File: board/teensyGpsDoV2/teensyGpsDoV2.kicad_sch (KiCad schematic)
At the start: 17 parts, among them J1 Barrel_Jack, J2 NPPN042AFCN-RC, SW1 SW_SPDT, U1 Teensy4.0, U2 LT1086-5.0, U3 DAC8550IxDGK, X1 OSC5A2B02

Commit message: Schematic WIP
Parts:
- added C5, C6: 1uF, symbol Device:C_Small_US
- added R7: 100, Resistor_THT:R_Axial_DIN0207_L6.3mm_D2.5mm_P7.62mm_Horizontal, symbol Device:R
- added TP1: 10 MHz TP, TestPoint:TestPoint_Pad_D2.0mm, symbol Connector:TestPoint
- added TP2: 5V TP, TestPoint:TestPoint_Pad_D2.0mm, symbol Connector:TestPoint
- added TP3: 1PPS TP, TestPoint:TestPoint_Pad_D2.0mm, symbol Connector:TestPoint
- added TP4: OSC VREF TP, TestPoint:TestPoint_Pad_D2.0mm, symbol Connector:TestPoint
- added U4: MCP1700x-330xxTO, Package_TO_SOT_THT:TO-92_Inline, symbol Regulator_Linear:MCP1700x-330xxTO
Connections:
- net +5V: now also C5.1, TP2.1, U4.2 (VI)
- net 10 MHz: now also R6.2, U1.26 (19_A5_SCL0)
- net GND: now also C5.2, C6.2, U4.1 (GND)
- net pps: now also U1.25 (18_A4_SDA0), R7.1, TP3.1; no longer J2.6, U1.9 (7_RX2_OUT1A)
- net at R1.2, R2.1, R6.1: now also TP1.1
- net at U1.11 (9_OUT1C): no longer R6.2
- net OSC VCTRL: now reaches U3.3 (V_{FB}), U3.4 (V_{OUT}), X1.3 (VCTRL)
- net OSC VCTRL: now also TP4.1
- net DAC VREF: now reaches U3.2 (V_{REF})
- net DAC VREF: now also C6.1, U4.3 (VO)
- new net: J2.6, R7.2
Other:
- note added: "1: VDD 2: VAnt 3: TxD 4: NC 5: RxD 6: PPS 7: NC 8: GND"
- moved on the sheet: J2, R1, R2, R6, U1, X1

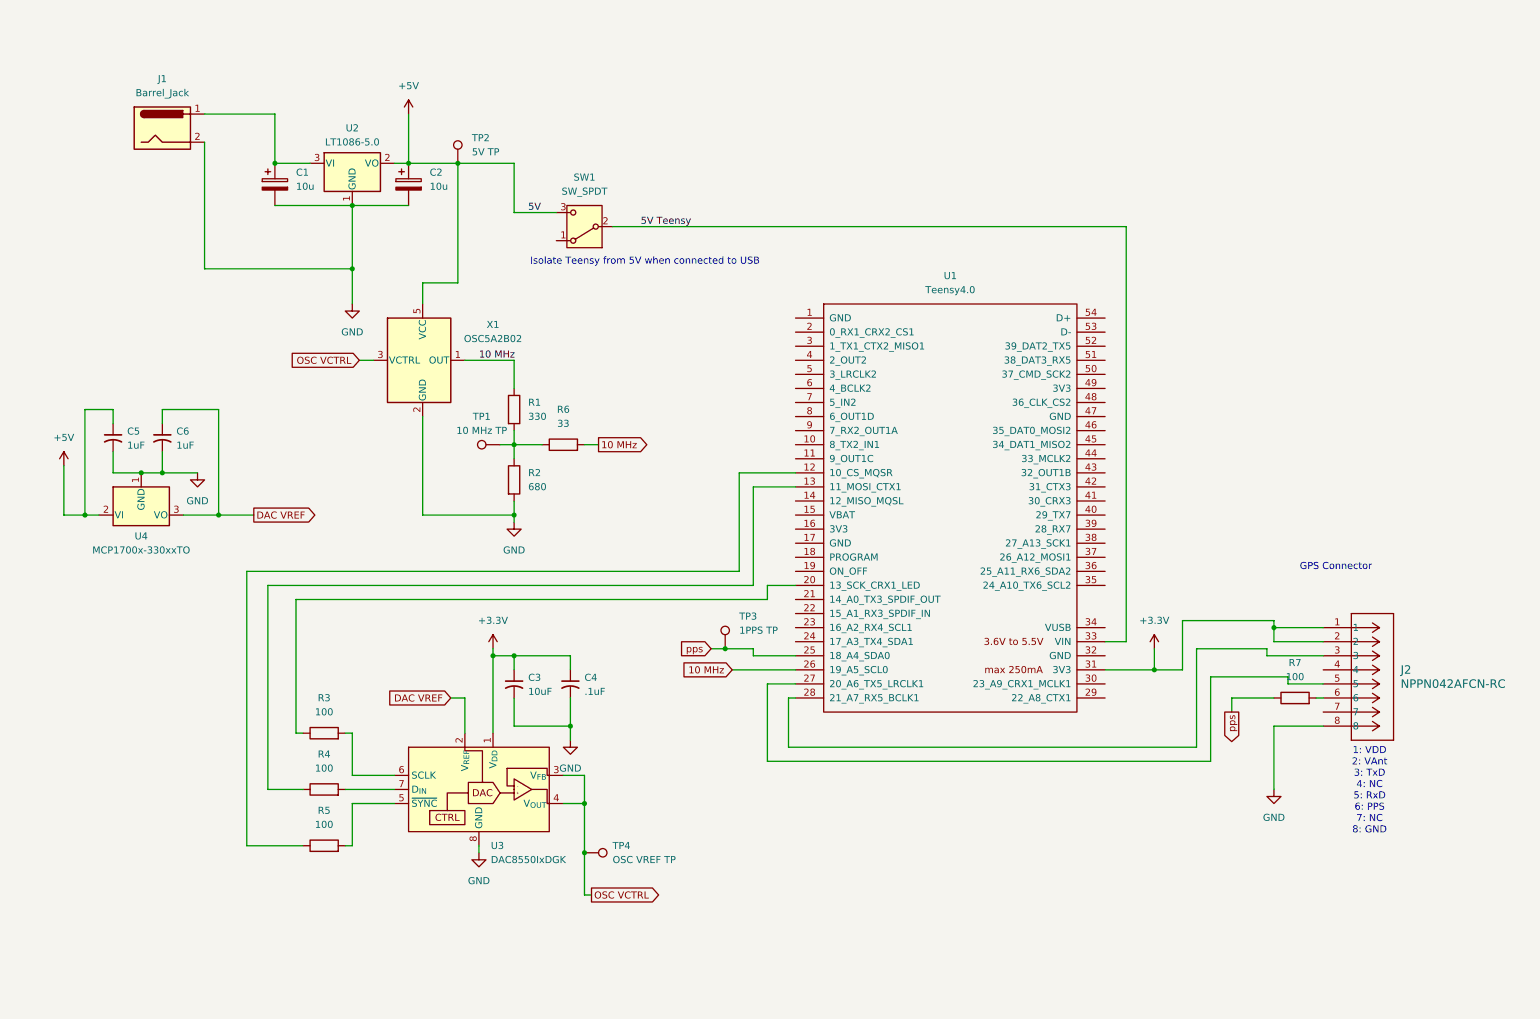
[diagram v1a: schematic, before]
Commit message: WIP, moved libraries to allow wire1 instead of wire modification. Lots of tuning. LCD optimations
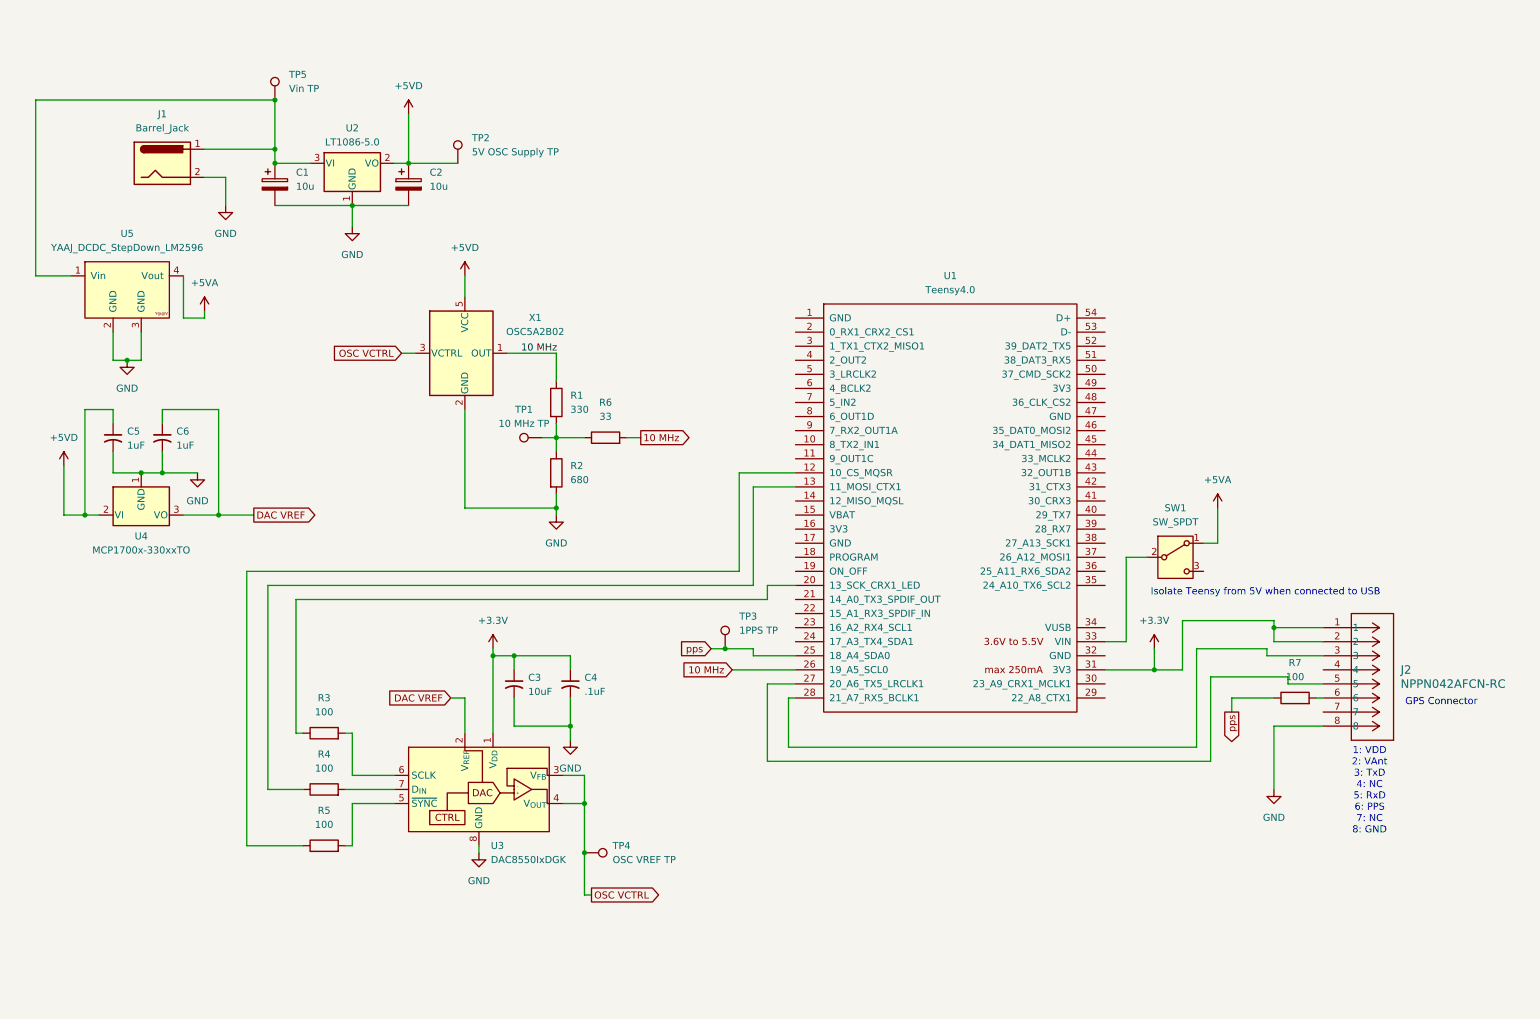
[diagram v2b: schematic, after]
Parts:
- added TP5: Vin TP, TestPoint:TestPoint_Pad_D2.0mm, symbol Connector:TestPoint
- added U5: YAAJ_DCDC_StepDown_LM2596, LM2596_Module:YAAJ_DCDC_StepDown_LM2596, symbol LM2596_Module:YAAJ_DCDC_StepDown_LM2596
- TP2: value 5V TP -> 5V OSC Supply TP
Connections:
- net GND: now also U5.2 (GND), U5.3 (GND)
- net at C1.1, J1.1, U2.3 (VI): now also TP5.1, U5.1 (Vin)
- net +5VA: now reaches SW1.1 (A)
- net +5VA: now also U5.4 (Vout)
- net +5V renamed +5VD
- net +5VD: no longer SW1.3 (C)
- net 5V Teensy: no longer names the net of SW1.2 (B), U1.33 (VIN)
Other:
- moved on the sheet: J1, R1, R2, R6, SW1, TP1, X1

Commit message: mobile update
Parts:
- added FB1, FB2: 133 @ 100 MHz, symbol Device:FerriteBead_Small
- added U6: 74HC14, Package_DIP:DIP-14_W7.62mm_Socket, symbol 74xx:74HC14
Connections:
- net +3.3V: now also FB1.1; no longer C3.1, C4.1, U3.1 (V_{DD})
- net +5VD: now also FB2.1; no longer X1.5 (VCC)
- new net: C3.1, C4.1, FB1.2, U3.1 (V_{DD})
- new net: FB2.2, X1.5 (VCC)

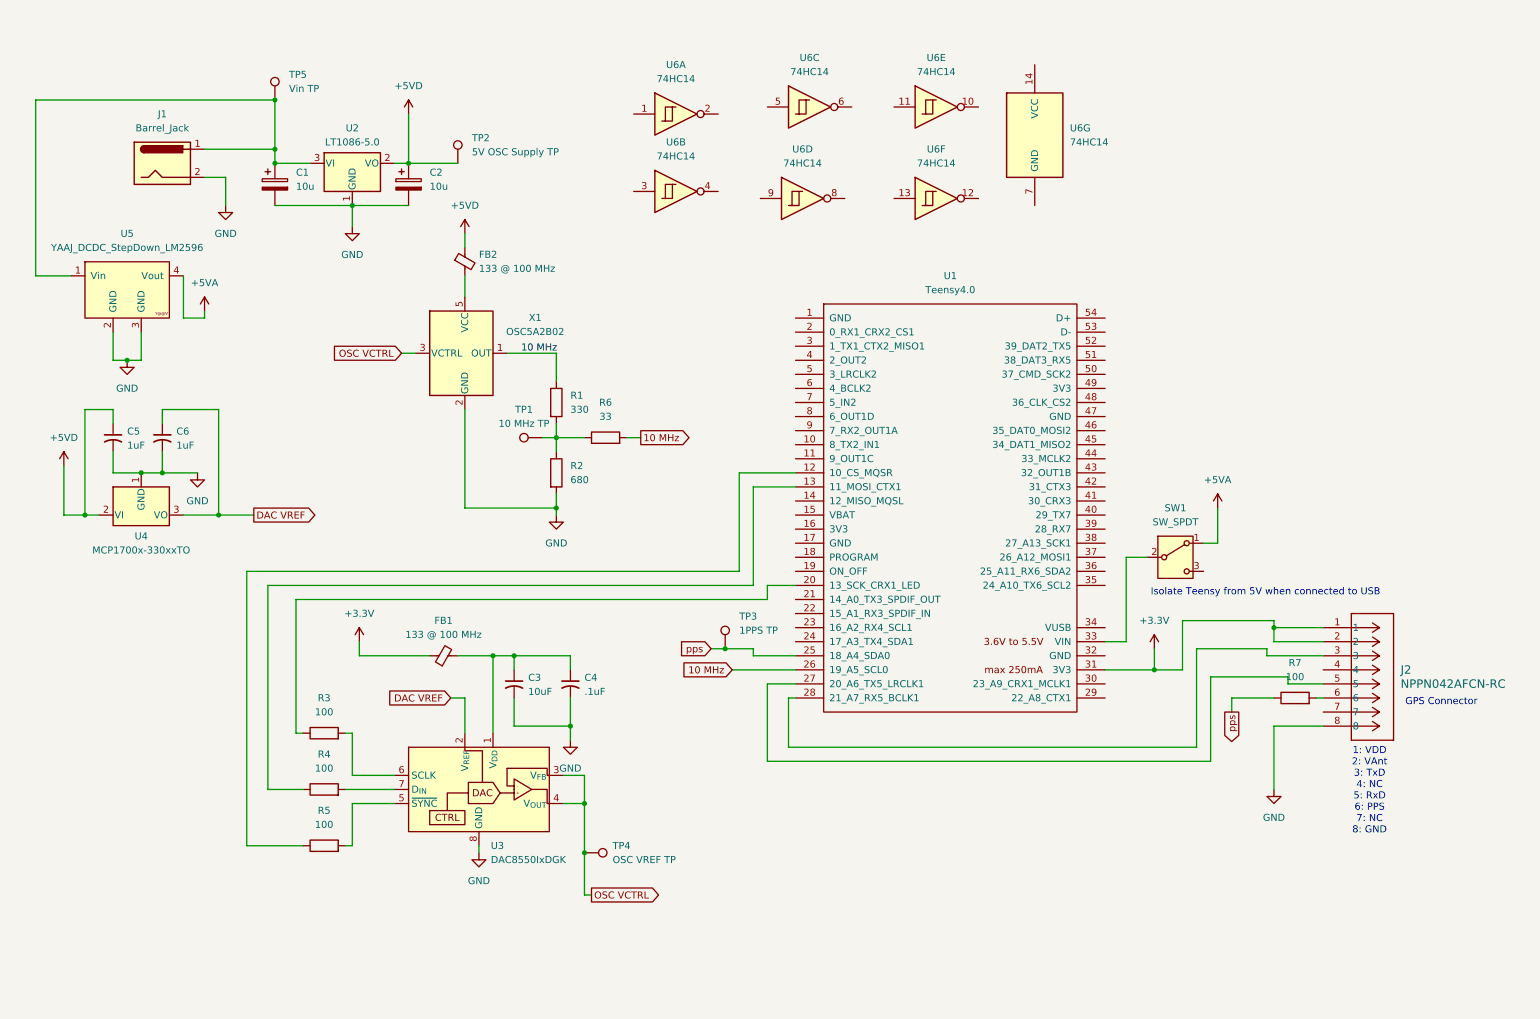
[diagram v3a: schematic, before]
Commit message: wip on schematic. Added PWM option instead of DAC
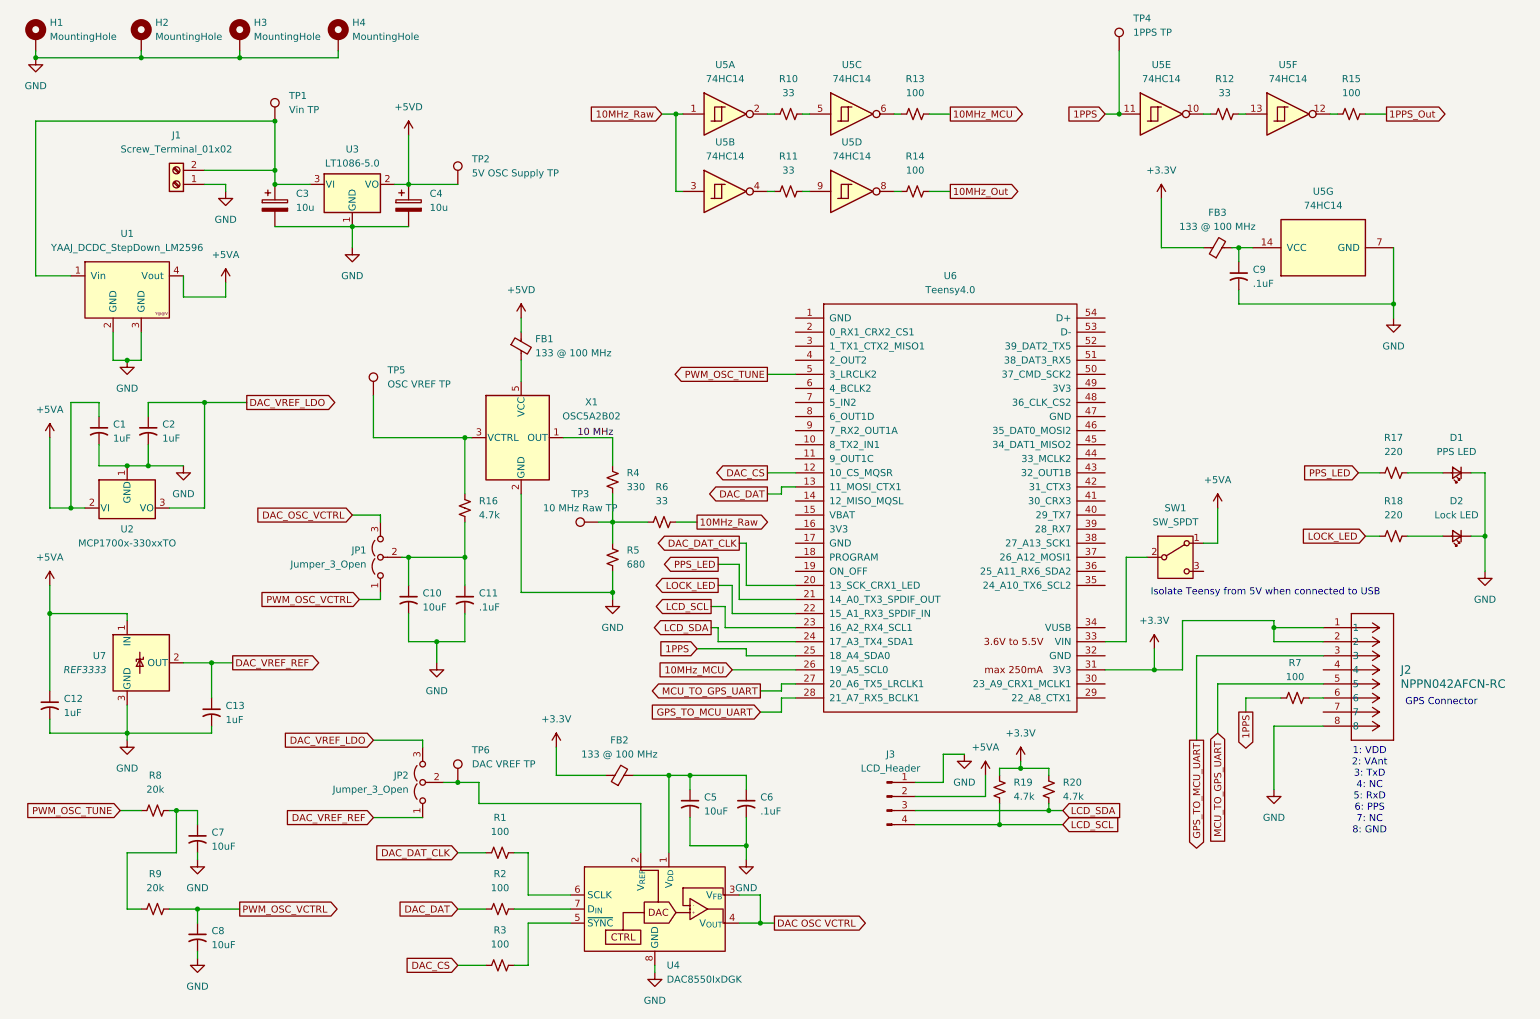
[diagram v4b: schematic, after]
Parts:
- removed J1: Barrel_Jack, Connector_BarrelJack:BarrelJack_SwitchcraftConxall_RAPC10U_Horizontal, symbol Connector:Barrel_Jack
- removed R1: 330, Resistor_THT:R_Axial_DIN0207_L6.3mm_D2.5mm_P7.62mm_Horizontal, symbol Device:R
- removed R2: 680, symbol Device:R
- removed R3, R4, R5, R7: 100, Resistor_THT:R_Axial_DIN0207_L6.3mm_D2.5mm_P7.62mm_Horizontal, symbol Device:R
- removed R6: 33, symbol Device:R
- added C10, C7, C8: 10uF, Capacitor_THT:C_Disc_D5.0mm_W2.5mm_P5.00mm, symbol Device:C_Small_US
- added C11, C9: .1uF, Capacitor_THT:C_Disc_D5.0mm_W2.5mm_P5.00mm, symbol Device:C_Small_US
- added C12, C13: 1uF, Capacitor_THT:C_Disc_D5.0mm_W2.5mm_P5.00mm, symbol Device:C_Small_US
- added D1: PPS LED, LED_THT:LED_D5.0mm_Clear, symbol Device:LED_Small
- added D2: Lock LED, LED_THT:LED_D5.0mm_Clear, symbol Device:LED_Small
- added FB3: 133 @ 100 MHz, Resistor_THT:R_Axial_DIN0411_L9.9mm_D3.6mm_P12.70mm_Horizontal, symbol Device:FerriteBead_Small
- added H1, H2, H3, H4: MountingHole, MountingHole:MountingHole_3.5mm_Pad, symbol Mechanical:MountingHole_Pad
- added J1: Screw_Terminal_01x02, TerminalBlock:TerminalBlock_MaiXu_MX126-5.0-02P_1x02_P5.00mm, symbol Connector:Screw_Terminal_01x02
- added J3: LCD_Header, Connector_PinHeader_2.54mm:PinHeader_1x04_P2.54mm_Vertical, symbol Connector:Conn_01x04_Pin
- added JP1, JP2: Jumper_3_Open, TestPoint:TestPoint_2Pads_Pitch5.08mm_Drill1.3mm, symbol Jumper:Jumper_3_Open
- added R1, R13, R14, R15, R2, R3, R7: 100, Resistor_THT:R_Axial_DIN0207_L6.3mm_D2.5mm_P10.16mm_Horizontal, symbol Device:R_Small_US
- added R10, R11, R12, R6: 33, Resistor_THT:R_Axial_DIN0207_L6.3mm_D2.5mm_P10.16mm_Horizontal, symbol Device:R_Small_US
- added R16, R19, R20: 4.7k, Resistor_THT:R_Axial_DIN0207_L6.3mm_D2.5mm_P10.16mm_Horizontal, symbol Device:R_Small_US
- added R17, R18: 220, Resistor_THT:R_Axial_DIN0207_L6.3mm_D2.5mm_P10.16mm_Horizontal, symbol Device:R_Small_US
- added R4: 330, Resistor_THT:R_Axial_DIN0207_L6.3mm_D2.5mm_P10.16mm_Horizontal, symbol Device:R_Small_US
- added R5: 680, Resistor_THT:R_Axial_DIN0207_L6.3mm_D2.5mm_P10.16mm_Horizontal, symbol Device:R_Small_US
- added R8, R9: 20k, Resistor_THT:R_Axial_DIN0207_L6.3mm_D2.5mm_P10.16mm_Horizontal, symbol Device:R_Small_US
- added TP6: DAC VREF TP, TestPoint:TestPoint_Pad_D2.0mm, symbol Connector:TestPoint
- added U7: REF3333, Package_TO_SOT_SMD:SOT-23, symbol Reference_Voltage:REF3033
- C1: renamed from C5; footprint (none) -> Capacitor_THT:C_Disc_D5.0mm_W2.5mm_P5.00mm
- C2: renamed from C6; footprint (none) -> Capacitor_THT:C_Disc_D5.0mm_W2.5mm_P5.00mm
- C5: renamed from C3; footprint (none) -> Capacitor_THT:C_Disc_D5.0mm_W2.5mm_P5.00mm
- C6: renamed from C4; footprint (none) -> Capacitor_THT:C_Disc_D5.0mm_W2.5mm_P5.00mm
- FB1: renamed from FB2; footprint (none) -> Resistor_THT:R_Axial_DIN0411_L9.9mm_D3.6mm_P12.70mm_Horizontal
- FB2: renamed from FB1; footprint (none) -> Resistor_THT:R_Axial_DIN0411_L9.9mm_D3.6mm_P12.70mm_Horizontal
- J2: footprint CONN4x2_NPPN042AFCN-RC_SUL -> NPPN042AFCN-RC:CONN4x2_NPPN042AFCN-RC_SUL
- SW1: footprint (none) -> Connector_PinSocket_2.54mm:PinSocket_1x03_P2.54mm_Vertical
- TP3: renamed from TP1; value 10 MHz TP -> 10 MHz Raw TP
- renumbered C1 to C3, C2 to C4, TP5 to TP1, TP3 to TP4, TP4 to TP5, U5 to U1, U4 to U2, U2 to U3, U3 to U4, U6 to U5, U1 to U6
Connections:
- net pps is gone; now on net 1PPS: TP4.1, U6.25 (18_A4_SDA0)
- net +3.3V: now also FB3.1, R19.1, R20.1
- net +5VA: now also C1.1, U2.2 (VI), C12.1, J3.2 (Pin_2), U7.1 (IN)
- net +5VD: no longer C1.1, U2.2 (VI)
- net 10 MHz: now also R4.1; no longer U6.26 (19_A5_SCL0)
- net GND: now also U5.7 (GND), C10.2, C11.2, C12.2, C13.2, C7.2, C8.2, C9.2, D1.1 (K), D2.1 (K), H1.1, H2.1, H3.1, H4.1, J1.1 (Pin_1), J3.1 (Pin_1), R5.2, U7.3 (GND)
- net at U5.5: now also R10.2
- net at U5.6: now also R13.1
- net DAC_DAT_CLK: now reaches U6.20 (13_SCK_CRX1_LED)
- net DAC_DAT_CLK: now also R1.1
- net at U4.6 (SCLK): now also R1.2
- net at TP3.1: now also R4.2, R5.1, R6.1
- net 10MHz_Raw: now reaches U5.1
- net 10MHz_Raw: now also U5.3, R6.2
- net at U5.2: now also R10.1
- net at C3.1, TP1.1, U1.1 (Vin)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: now also J1.2 (Pin_2)
- net GPS_TO_MCU_UART: now reaches J2.3, U6.28 (21_A7_RX5_BCLK1)
- net MCU_TO_GPS_UART: now reaches J2.5, U6.27 (20_A6_TX5_LRCLK1)
- net at J2.6: now also R7.2
- net DAC_DAT: now reaches U6.13 (11_MOSI_CTX1)
- net DAC_DAT: now also R2.1
- net at U4.7 (D_{IN}): now also R2.2
- net at U5.12: now also R15.1
- net at U5.13: now also R12.2
- net at U5.10: now also R12.1
- net 1PPS: now reaches U5.11
- net 1PPS: now also R7.1
- net at U4.5 (~{SYNC}): now also R3.2
- net at U5.14 (VCC): now also C9.1, FB3.2
- net DAC_CS: now reaches U6.12 (10_CS_MQSR)
- net DAC_CS: now also R3.1
- net PPS_LED: now reaches U6.21 (14_A0_TX3_SPDIF_OUT)
- net PPS_LED: now also R17.1
- net LOCK_LED: now reaches U6.22 (15_A1_RX3_SPDIF_IN)
- net LOCK_LED: now also R18.1
- net LCD_SCL: now reaches U6.23 (16_A2_RX4_SCL1)
- net LCD_SCL: now also J3.4 (Pin_4), R19.2
- net LCD_SDA: now reaches U6.24 (17_A3_TX4_SDA1)
- net LCD_SDA: now also J3.3 (Pin_3), R20.2
- net PWM_OSC_TUNE: now reaches U6.5 (3_LRCLK2)
- net PWM_OSC_TUNE: now also R8.2
- net at U5.8: now also R14.1
- net at U5.9: now also R11.2
- net at U5.4: now also R11.1
- net DAC VREF renamed DAC_VREF_LDO
- net DAC_VREF_LDO: now also JP2.3 (B); no longer U4.2 (V_{REF})
- net OSC VCTRL: no longer names the net of TP5.1, X1.3 (VCTRL)
- net OSC VCTRL: now also R16.1; no longer U4.3 (V_{FB}), U4.4 (V_{OUT})
- new net: C7.1, R8.1, R9.1
- new net: JP2.2 (C), TP6.1, U4.2 (V_{REF})
- new net: D2.2 (A), R18.2
- new net: C10.1, C11.1, JP1.2 (C), R16.2
- new net: D1.2 (A), R17.2
- new net 10MHz_MCU: R13.2, U6.26 (19_A5_SCL0)
- new net 10MHz_Out: R14.2
- new net 1PPS_Out: R15.2
- new net DAC OSC VCTRL: U4.3 (V_{FB}), U4.4 (V_{OUT})
- new net DAC_OSC_VCTRL: JP1.3 (B)
- new net DAC_VREF_REF: C13.1, JP2.1 (A), U7.2 (OUT)
- new net PWM_OSC_VCTRL: C8.1, JP1.1 (A), R9.2
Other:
- moved on the sheet: C1, C2, C3, C4, C5, C6, FB1, FB2, TP1, TP2, TP3, TP4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

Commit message: layout wip
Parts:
- removed TP1: Vin TP, TestPoint:TestPoint_Pad_D2.0mm, symbol Connector:TestPoint
- removed TP2: 5V OSC Supply TP, TestPoint:TestPoint_Pad_D2.0mm, symbol Connector:TestPoint
- removed TP3: 10 MHz Raw TP, TestPoint:TestPoint_Pad_D2.0mm, symbol Connector:TestPoint
- removed TP4: 1PPS TP, TestPoint:TestPoint_Pad_D2.0mm, symbol Connector:TestPoint
- removed TP5: OSC VREF TP, TestPoint:TestPoint_Pad_D2.0mm, symbol Connector:TestPoint
- removed TP6: DAC VREF TP, TestPoint:TestPoint_Pad_D2.0mm, symbol Connector:TestPoint
- added J4: 10MHz Out, Connector_Coaxial:SMA_Wurth_60312002114503_Vertical, symbol Connector:Conn_Coaxial_Small
- added J5: 1PPS Out, Connector_Coaxial:SMA_Wurth_60312002114503_Vertical, symbol Connector:Conn_Coaxial_Small
- J2: value NPPN042AFCN-RC -> GPS Connector
- JP1: value Jumper_3_Open -> OSC_VCTRL_SEL; footprint TestPoint:TestPoint_2Pads_Pitch5.08mm_Drill1.3mm -> Connector_PinHeader_2.54mm:PinHeader_1x03_P2.54mm_Vertical
- JP2: value Jumper_3_Open -> DAC_VREF_SEL; footprint TestPoint:TestPoint_2Pads_Pitch5.08mm_Drill1.3mm -> Connector_PinHeader_2.54mm:PinHeader_1x03_P2.54mm_Vertical
- U1: value YAAJ_DCDC_StepDown_LM2596 -> LM2596_Module
- U2: value MCP1700x-330xxTO -> MCP1703
- U4: value DAC8550IxDGK -> DAC8550
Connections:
- net 10 MHz: no longer names the net of R4.1, X1.1 (OUT)
- net 10MHz_Out: no longer names the net of R14.2
- net 10MHz_Out: now also J4.1 (In)
- net 1PPS_Out: no longer names the net of R15.2
- net 1PPS_Out: now also J5.1 (In)
